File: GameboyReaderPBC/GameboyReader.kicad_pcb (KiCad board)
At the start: 2 copper layers, 93 x 75 mm, 13 parts, among them J1 Conn_01x32_Male, U1 74HC595, U2 74HC595

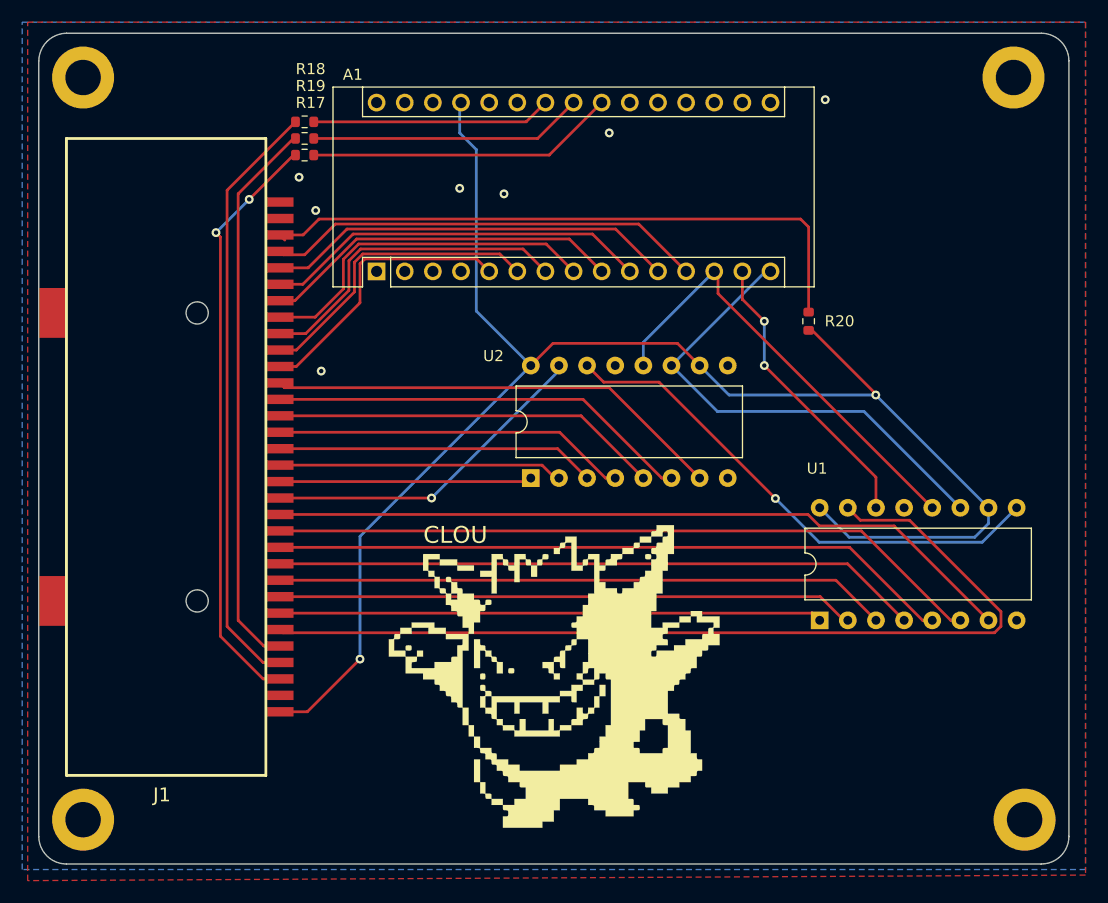
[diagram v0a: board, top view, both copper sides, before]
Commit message: kicad: updated versions extensions
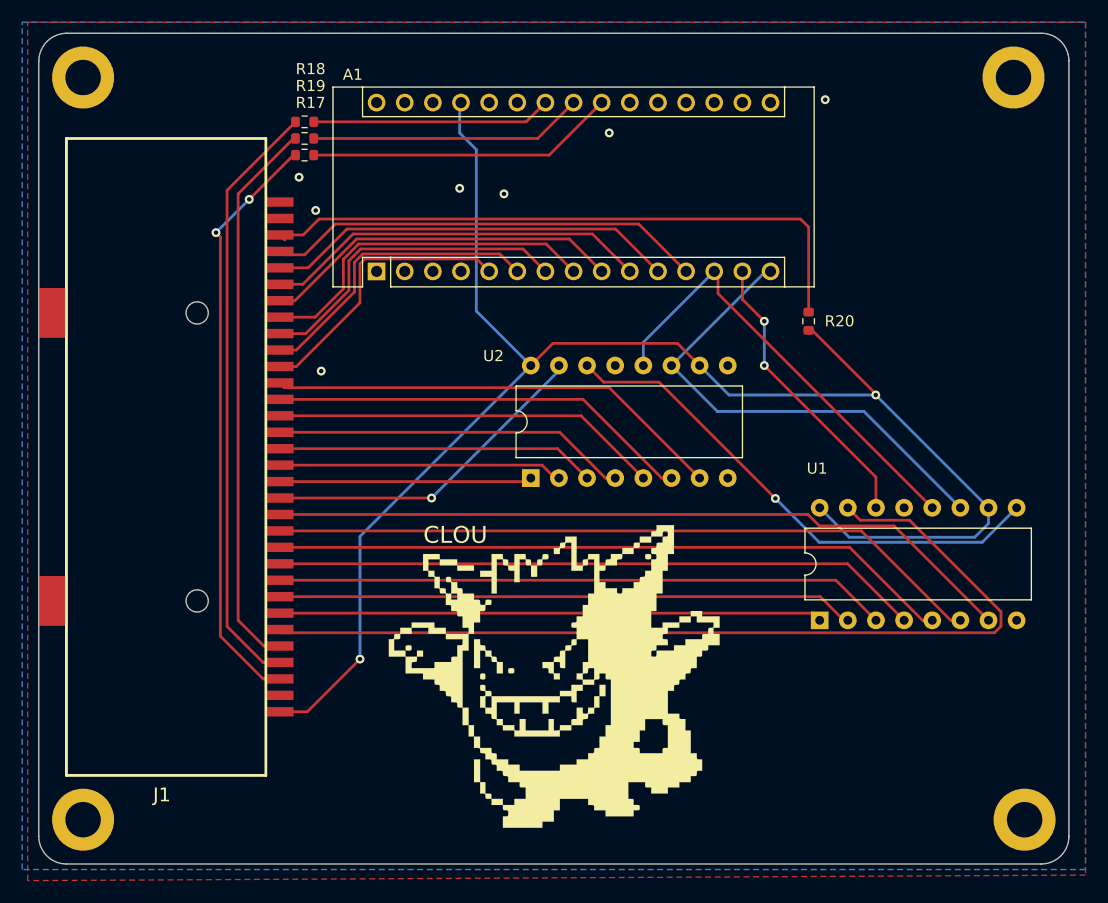
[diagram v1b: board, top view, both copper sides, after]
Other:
- net class Default removed
